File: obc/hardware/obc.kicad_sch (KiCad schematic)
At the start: 0 parts

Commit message: add power domain
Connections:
- no-connect marks 0 -> 7
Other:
- added sheet Inter-Board-Connector (inter_board_connector.kicad_sch)

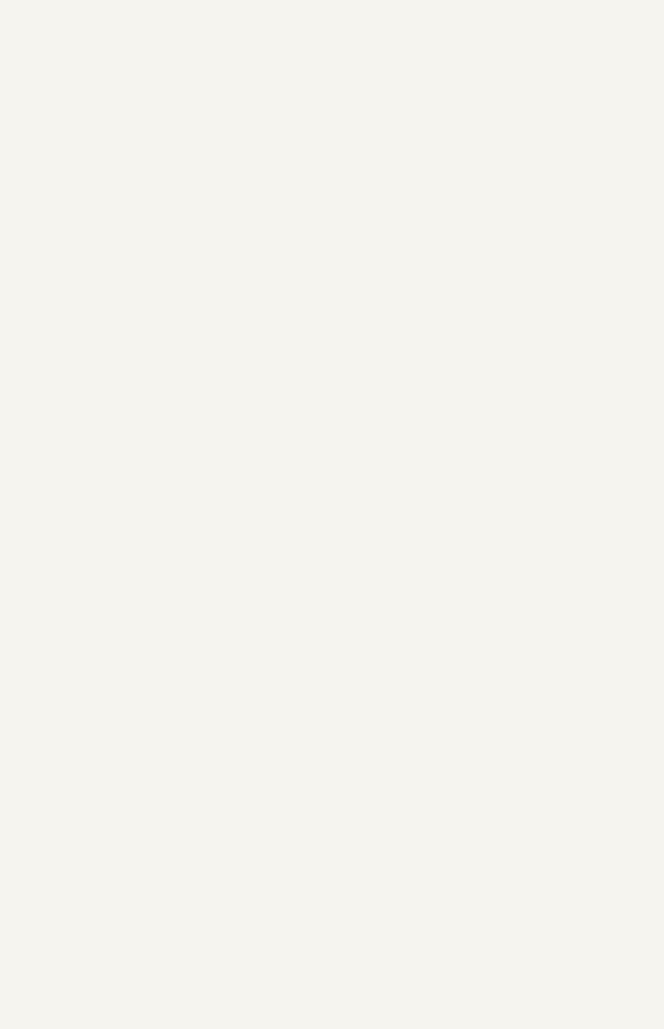
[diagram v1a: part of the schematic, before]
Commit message: add stm32h7
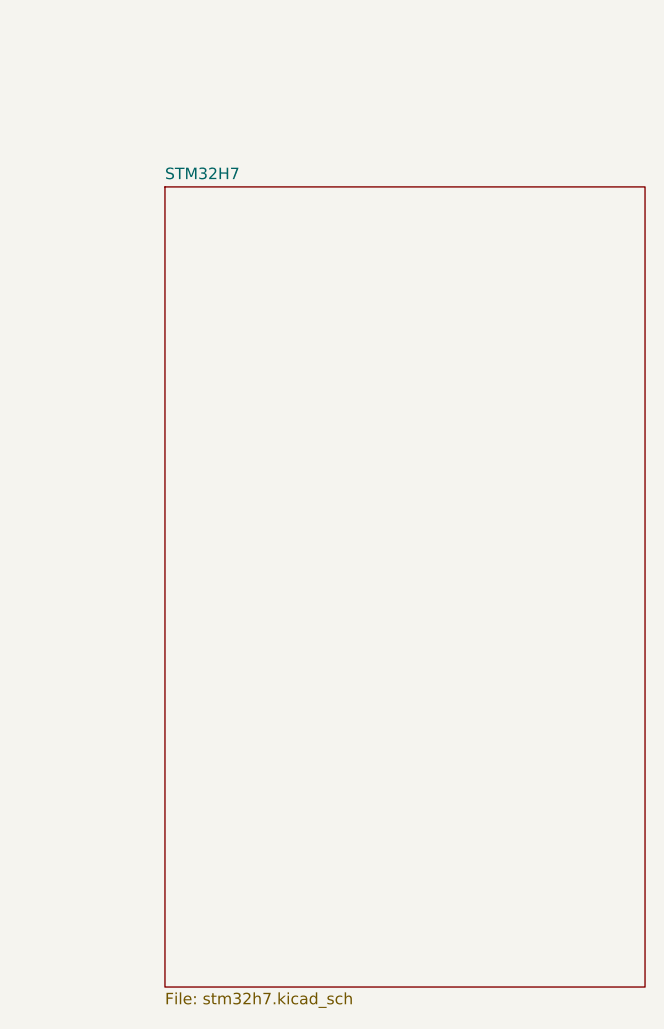
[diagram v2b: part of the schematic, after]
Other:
- added sheet STM32H7 (stm32h7.kicad_sch)
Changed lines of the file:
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@@
+	)
+	(sheet
+		(at 85.09 82.55)
+		(size 53.34 88.9)
+		(exclude_from_sim no)
+		(in_bom yes)
+		(on_board yes)
+		(dnp no)
+		(fields_autoplaced yes)
+		(stroke
+			(width 0.1524)
+			(type solid)
+		)
+		(fill
+			(color 0 0 0 0.0000)
+		)
+		(property "Sheetname" "STM32H7"
+			(at 85.09 81.8384 0)
+			(effects
+				(font
+					(size 1.27 1.27)
+				)
+				(justify left bottom)
+			)
+		)
+		(property "Sheetfile" "stm32h7.kicad_sch"
+			(at 85.09 172.0346 0)
+			(effects
+				(font
+					(size 1.27 1.27)
+				)
+				(justify left top)
+			)
+		)
+		(instances
+			(project "obc"
+				(path "/ba4f88ff-24aa-49a3-8871-8c7e48b371c5"
+					(page "3")
+				)
+			)
+		)
 	)
 	(sheet

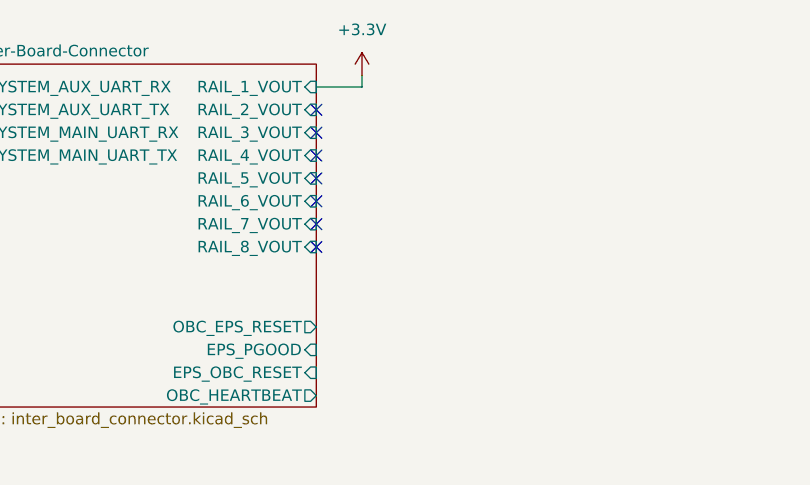
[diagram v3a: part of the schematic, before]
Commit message: add RTC battery and sensors, preliminary layout
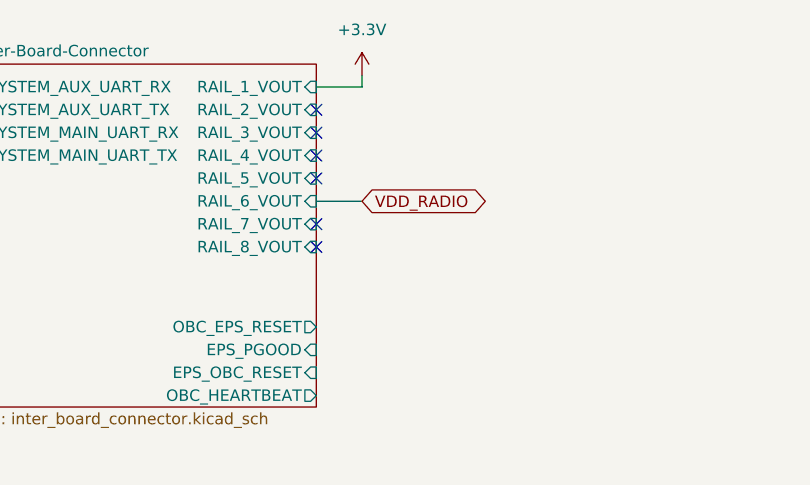
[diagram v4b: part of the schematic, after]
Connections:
- no-connect marks 7 -> 6
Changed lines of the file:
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@@
-	)
-	(no_connect
-		(at 53.34 34.29)
 	)
 	(no_connect
@@
 		)
 	)
+	(wire
+		(pts
+			(xy 53.34 34.29) (xy 58.42 34.29)
+		)
+		(stroke
+			(width 0)
+			(type default)
+		)
+	)
+	(global_label "VDD_RADIO"
+		(shape bidirectional)
+		(at 58.42 34.29 0)
+		(fields_autoplaced yes)
+		(effects
+			(font
+				(size 1.27 1.27)
+			)
+			(justify left)
+		)
+		(property "Intersheetrefs" "${INTERSHEET_REFS}"
+			(at 72.6766 34.29 0)
+			(hide yes)
+			(show_name no)
+			(do_not_autoplace no)
+			(effects
+				(font
+					(size 1.27 1.27)
+				)
+				(justify left)
+			)
+		)
+	)

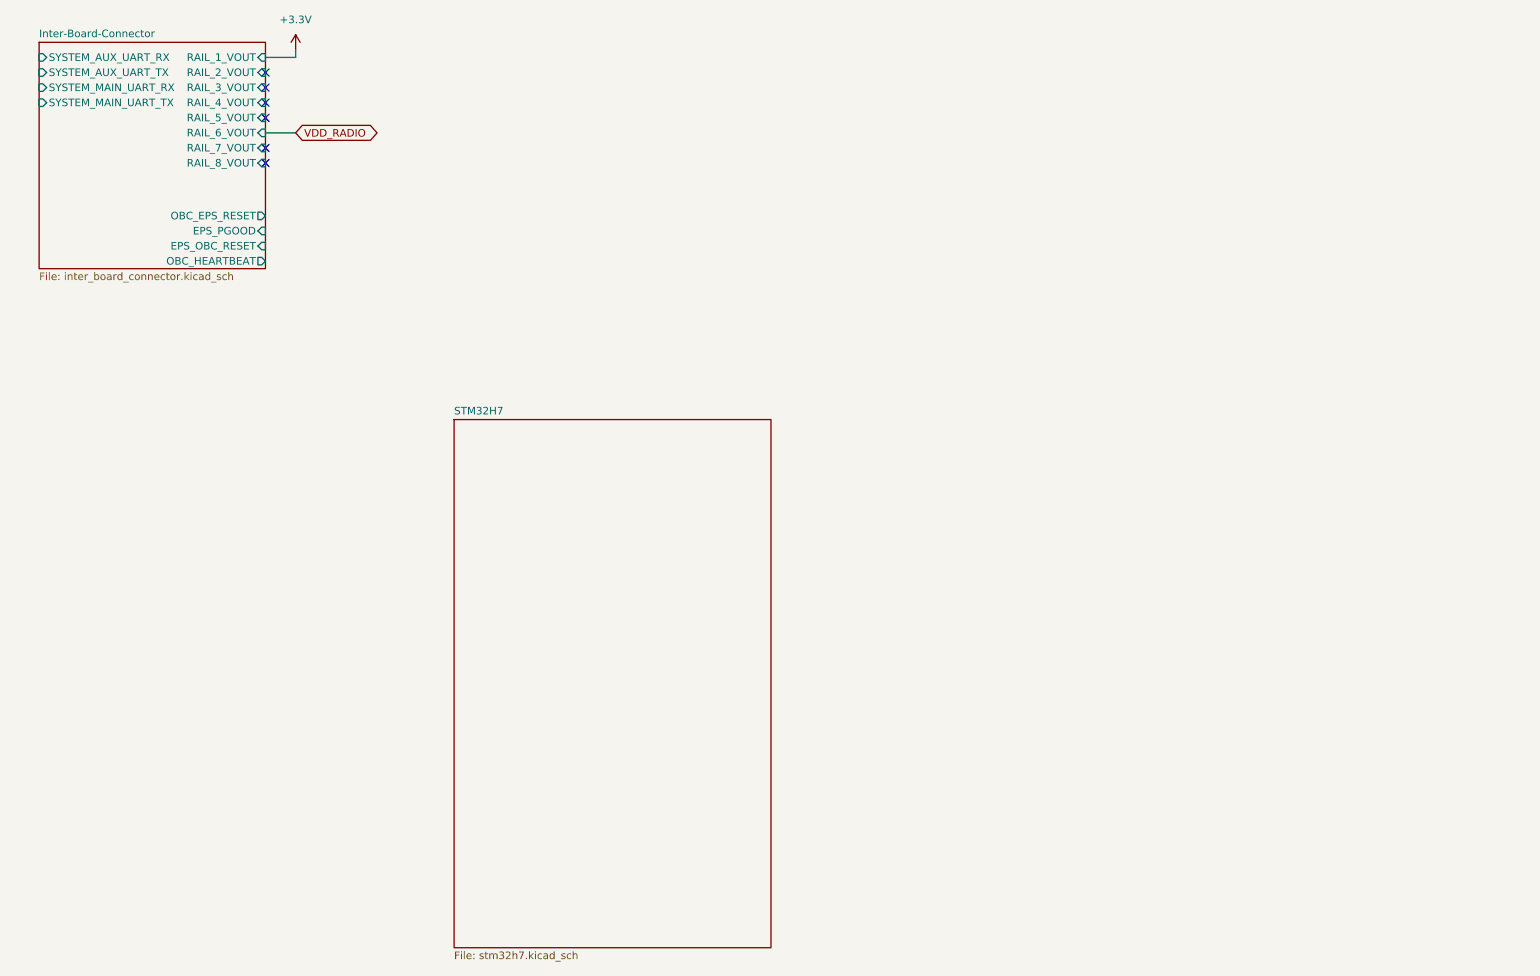
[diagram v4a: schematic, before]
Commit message: added CAN, UART, supervisor, USB, power OR-ing, GPS, did layout
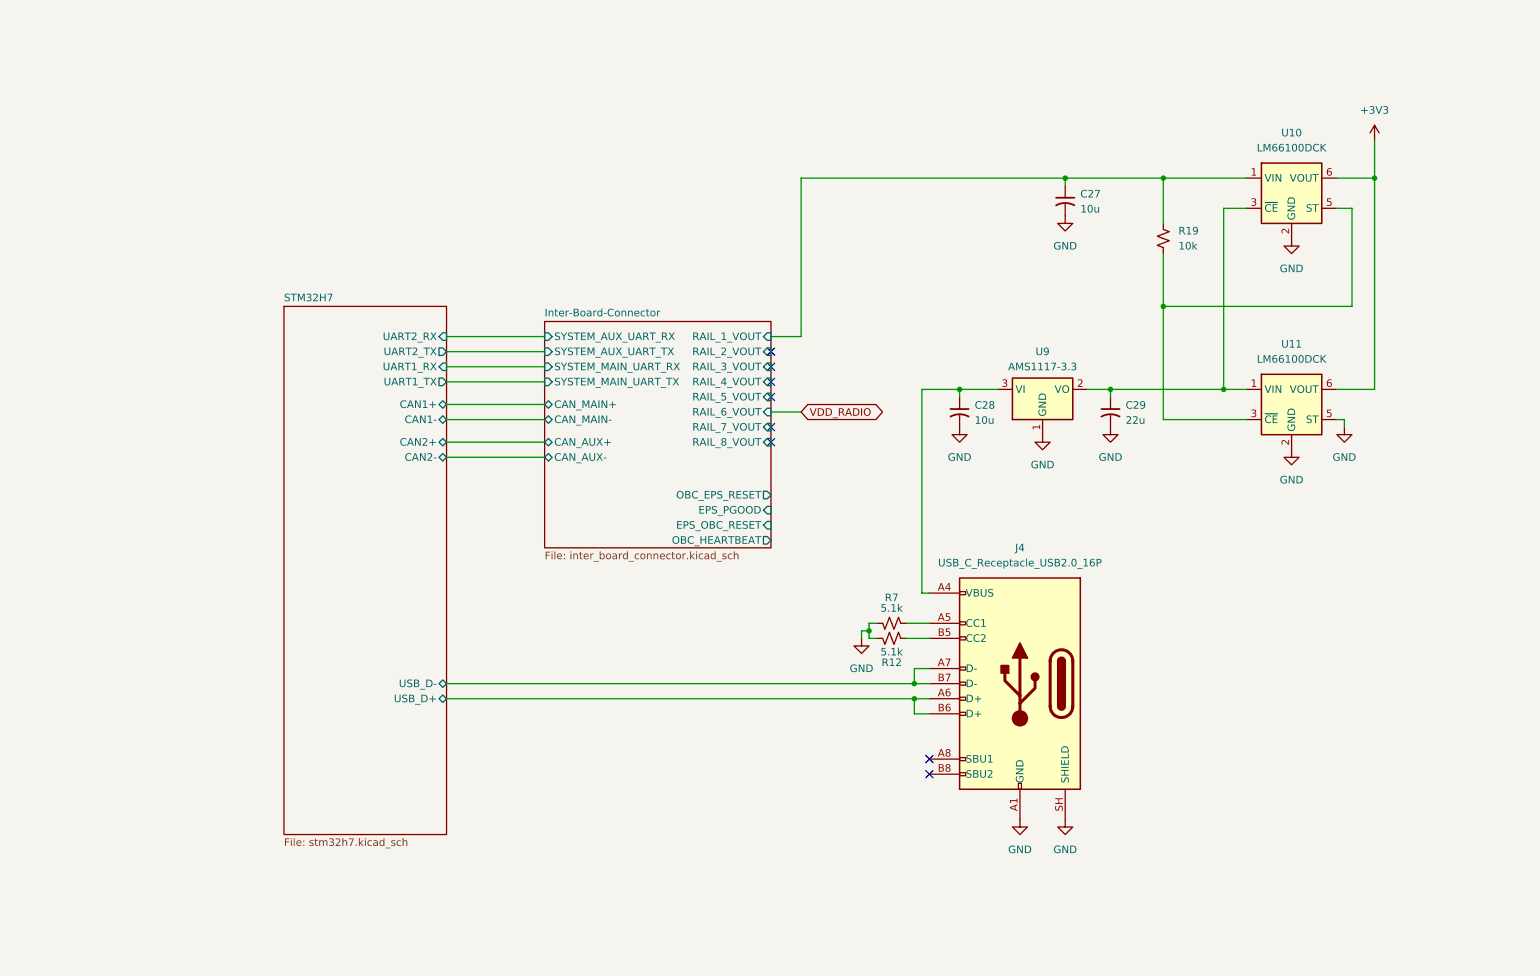
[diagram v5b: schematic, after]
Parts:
- added C27, C28: 10u, Capacitor_SMD:C_0402_1005Metric, symbol Device:C_Small_US
- added C29: 22u, Capacitor_SMD:C_0603_1608Metric, symbol Device:C_Small_US
- added J4: USB_C_Receptacle_USB2.0_16P, Connector_USB:USB_C_Receptacle_G-Switch_GT-USB-7010ASV, symbol Connector:USB_C_Receptacle_USB2.0_16P
- added R12, R7: 5.1k, Resistor_SMD:R_0402_1005Metric, symbol Device:R_Small_US
- added R19: 10k, Resistor_SMD:R_0402_1005Metric, symbol Device:R_Small_US
- added U10, U11: LM66100DCK, Package_TO_SOT_SMD:SOT-363_SC-70-6, symbol Power_Management:LM66100DCK
- added U9: AMS1117-3.3, Package_TO_SOT_SMD:SOT-223-3_TabPin2, symbol Regulator_Linear:AMS1117-3.3
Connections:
- new net: C29.1, U10.3 (~{CE}), U11.1 (VIN), U9.2 (VO)
- new net: R19.2, U10.5 (ST), U11.3 (~{CE})
- new net: C28.1, J4.A4 (VBUS), J4.A9 (VBUS), J4.B4 (VBUS), J4.B9 (VBUS), U9.3 (VI)
- new net: J4.A5 (CC1), R7.1
- new net: J4.B5 (CC2), R12.2
- new net +3V3: U10.6 (VOUT), U11.6 (VOUT)
- new net GND: C27.2, C28.2, C29.2, J4.A1 (GND), J4.A12 (GND), J4.B1 (GND), J4.B12 (GND), J4.SH (SHIELD), R12.1, R7.2, U10.2 (GND), U11.2 (GND), U11.5 (ST), U9.1 (GND)
- new net Inter-Board-Connector/RAIL_1_VOUT: C27.1, R19.1, U10.1 (VIN)
- new net STM32H7/USB_D+: J4.A6 (D+), J4.B6 (D+)
- new net STM32H7/USB_D-: J4.A7 (D-), J4.B7 (D-)
- no-connect marks 6 -> 8
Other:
- sheet Inter-Board-Connector ports: added CAN_AUX+, CAN_AUX-, CAN_MAIN+, CAN_MAIN-; removed none
- sheet STM32H7 ports: added CAN1+, CAN1-, CAN2+, CAN2-, UART1_RX, UART1_TX, UART2_RX, UART2_TX, USB_D+, USB_D-; removed none

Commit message: add SCRT and OSU AIAA logos, add IMU, add PPS LED, hook up some IOs
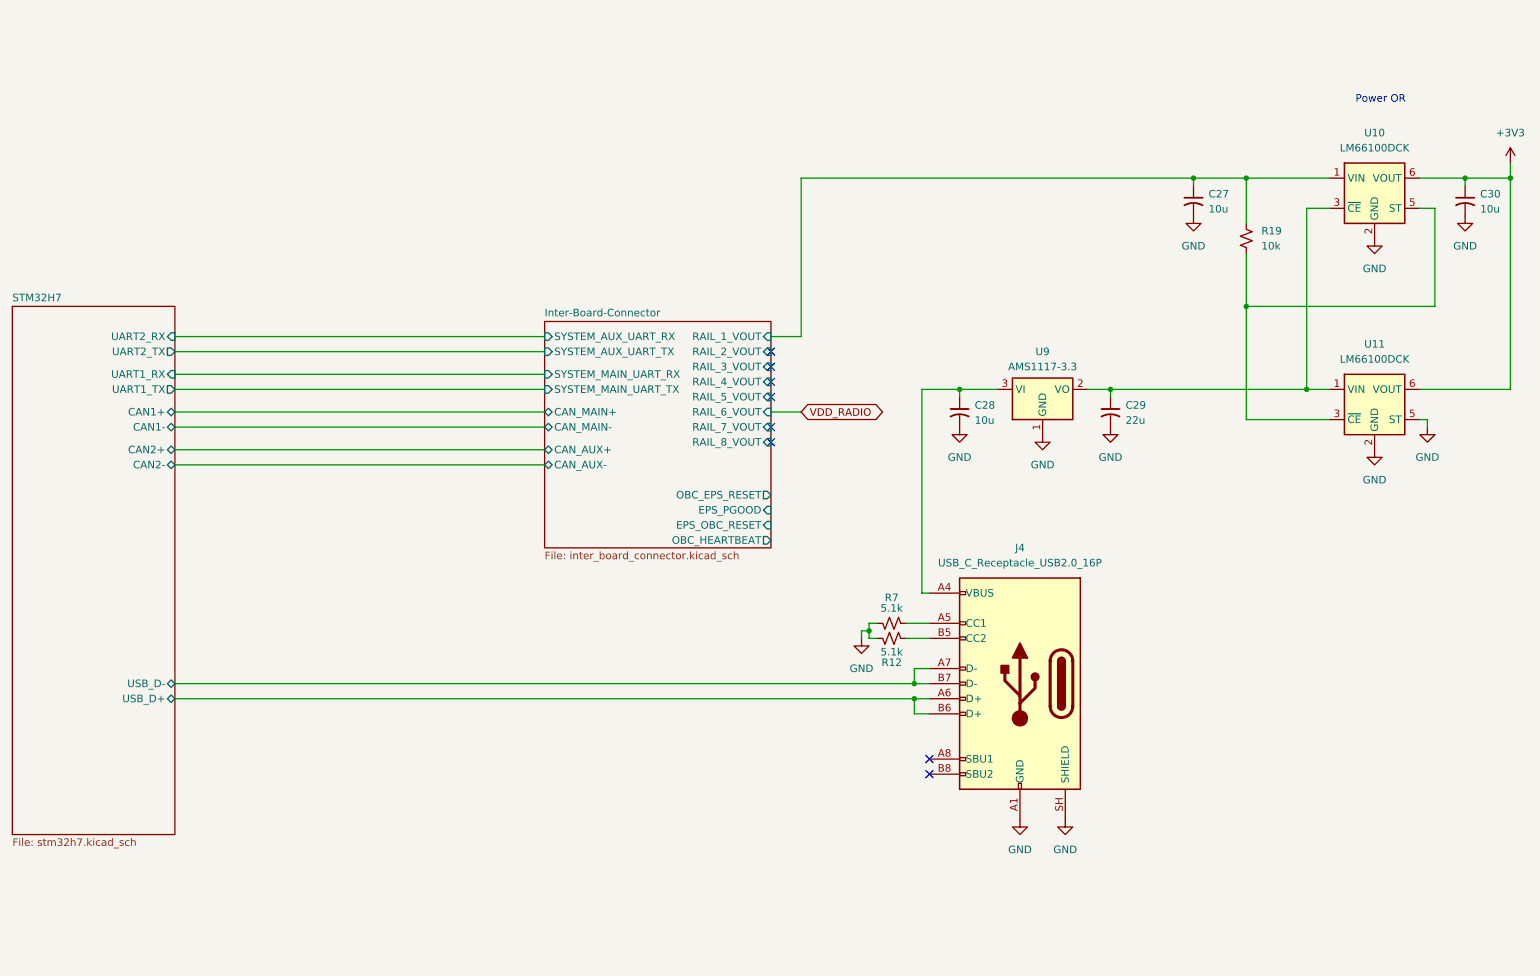
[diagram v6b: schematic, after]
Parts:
- added C30: 10u, Capacitor_SMD:C_0402_1005Metric, symbol Device:C_Small_US
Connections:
- net +3V3: now also C30.1
- net GND: now also C30.2
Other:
- note added: "Power OR"
- moved on the sheet: C27, R19, U10, U11

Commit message: add antenna supervisor, ESD, reroute some stuff
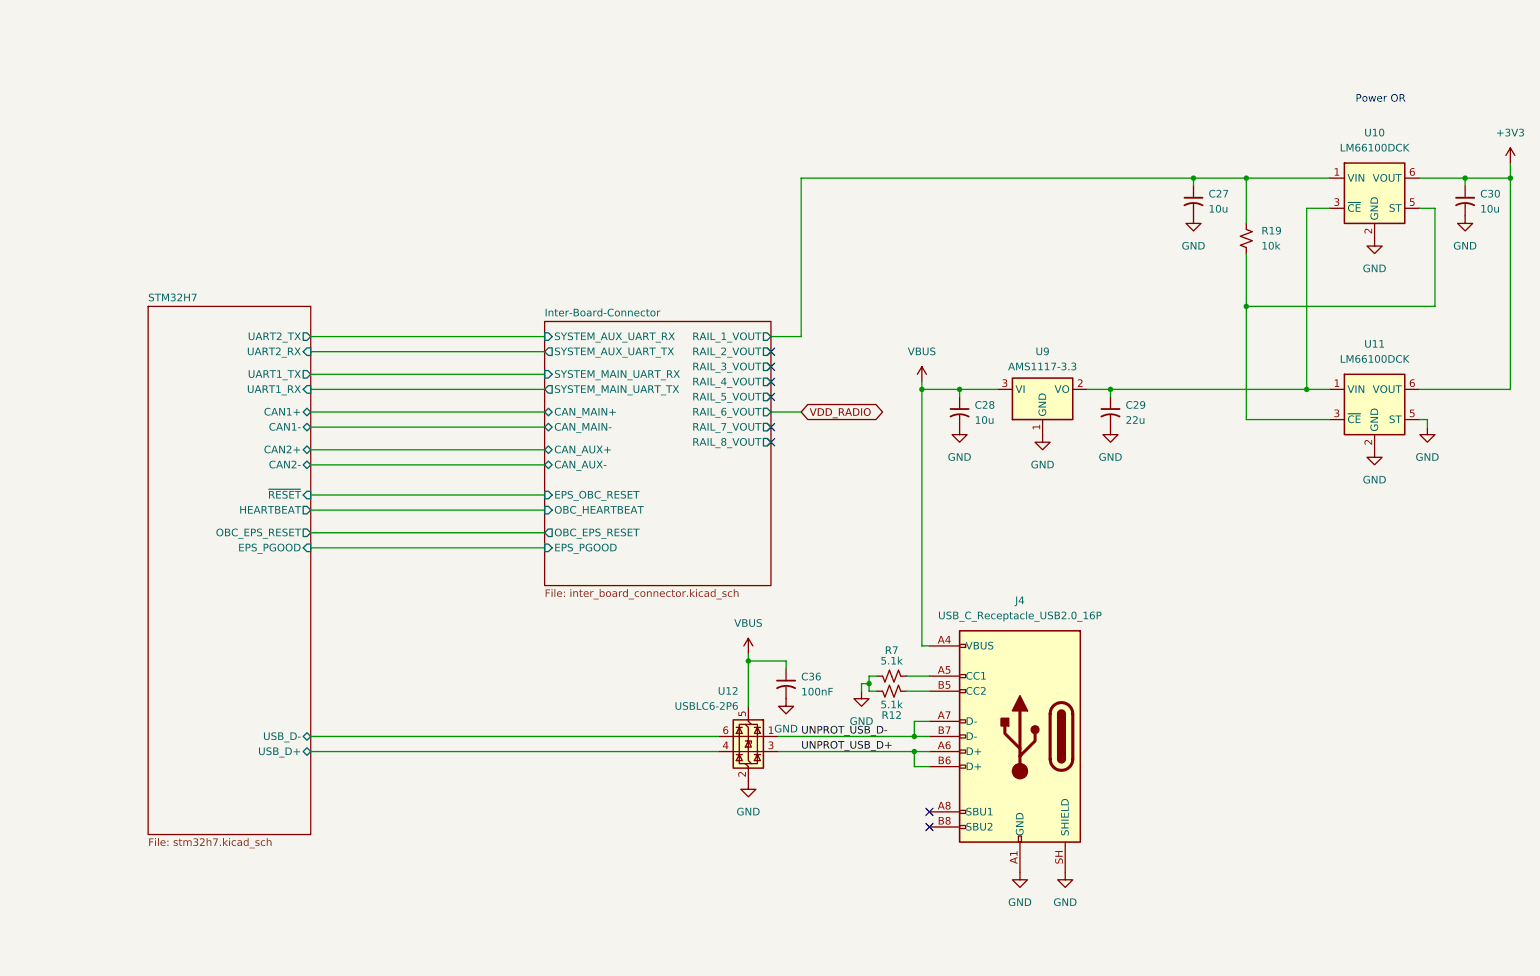
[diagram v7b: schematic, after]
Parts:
- added C36: 100nF, Capacitor_SMD:C_0402_1005Metric, symbol Device:C_Small_US
- added U12: USBLC6-2P6, Package_TO_SOT_SMD:SOT-666, symbol Power_Protection:USBLC6-2P6
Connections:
- net GND: now also C36.2, U12.2 (GND)
- net STM32H7/USB_D+: now also U12.4 (I/O2); no longer J4.A6 (D+), J4.B6 (D+)
- net STM32H7/USB_D-: now also U12.6 (I/O1); no longer J4.A7 (D-), J4.B7 (D-)
- net VBUS: now reaches C28.1, J4.A4 (VBUS), J4.A9 (VBUS), J4.B4 (VBUS), J4.B9 (VBUS), U9.3 (VI)
- net VBUS: now also C36.1, U12.5 (VBUS)
- new net UNPROT_USB_D+: J4.A6 (D+), J4.B6 (D+), U12.3 (I/O2)
- new net UNPROT_USB_D-: J4.A7 (D-), J4.B7 (D-), U12.1 (I/O1)
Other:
- sheet STM32H7 ports: added EPS_PGOOD, HEARTBEAT, OBC_EPS_RESET, ~{RESET}; removed none
- moved on the sheet: J4, R12, R7

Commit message: cleanup
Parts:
- C27, C28, C30: value 10u -> 10uF; footprint Capacitor_SMD:C_0402_1005Metric -> Capacitor_SMD:C_0603_1608Metric; LCSC (none) -> C19702
- C29: LCSC (none) -> C59461
- C36: LCSC (none) -> C1525
- J4: LCSC (none) -> C2988369
- R12, R7: LCSC (none) -> C25905
- R19: LCSC (none) -> C25744
- U10, U11: LCSC (none) -> C5219211
- U12: LCSC (none) -> C15999
- U9: LCSC (none) -> C6186
